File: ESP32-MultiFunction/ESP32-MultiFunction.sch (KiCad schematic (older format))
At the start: 8 parts, among them U0 ESP32_DEVKIT_C

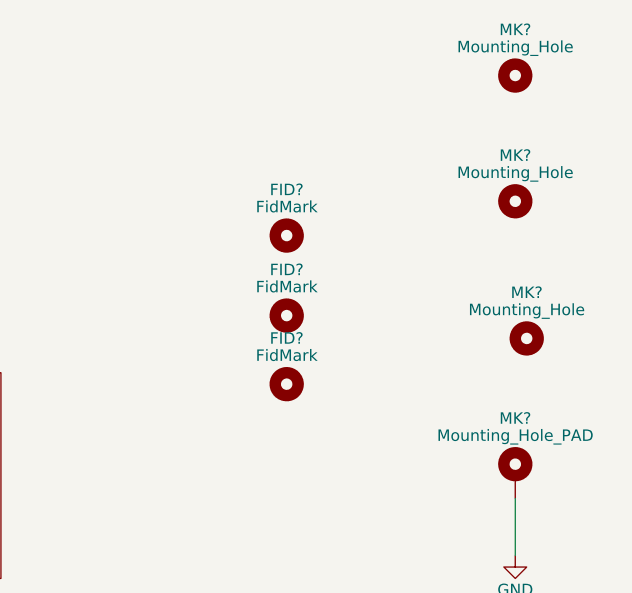
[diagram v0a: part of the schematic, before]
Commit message: Working on ESP32-MultiFunction.
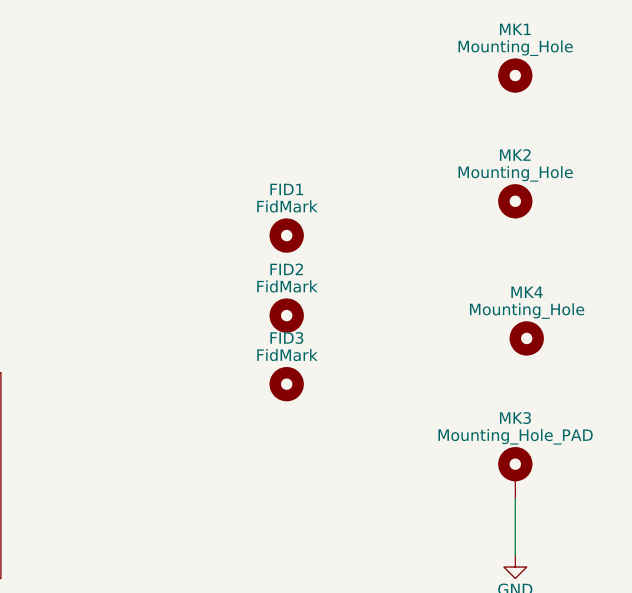
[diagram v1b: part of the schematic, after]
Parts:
- FID1, FID2, FID3: renamed from FID?; footprint (none) -> Fiducials:Fiducial_1mm_Dia_2.54mm_Outer_CopperBottom
- MK1, MK2, MK4: renamed from MK?; footprint (none) -> Mounting_Holes:MountingHole_3.2mm_M3
- MK3: renamed from MK?; footprint (none) -> Mounting_Holes:MountingHole_3.2mm_M3_Pad
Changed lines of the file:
@@
 $Descr A4 11693 8268
 encoding utf-8
-Sheet 1 7
+Sheet 1 8
 Title "ESP32 Multifunction board"
 Date ""
@@
 $EndComp
 $Comp
-L GND #PWR?
+L GND #PWR5
 U 1 1 60CCB9BA
 P 3900 2300
-F 0 "#PWR?" H 3900 2050 50  0001 C CNN
+F 0 "#PWR5" H 3900 2050 50  0001 C CNN
 F 1 "GND" H 3900 2150 50  0000 C CNN
 F 2 "" H 3900 2300 50  0001 C CNN
@@
 $EndComp
 $Comp
-L GND #PWR?
+L GND #PWR4
 U 1 1 60CCB9E8
 P 3900 2000
-F 0 "#PWR?" H 3900 1750 50  0001 C CNN
+F 0 "#PWR4" H 3900 1750 50  0001 C CNN
 F 1 "GND" H 3900 1850 50  0000 C CNN
 F 2 "" H 3900 2000 50  0001 C CNN
@@
 $EndComp
 $Comp
-L GND #PWR?
+L GND #PWR3
 U 1 1 60CCBA16
 P 2800 2650
-F 0 "#PWR?" H 2800 2400 50  0001 C CNN
+F 0 "#PWR3" H 2800 2400 50  0001 C CNN
 F 1 "GND" H 2800 2500 50  0000 C CNN
 F 2 "" H 2800 2650 50  0001 C CNN
@@
 $EndComp
 $Comp
-L +3V3 #PWR?
+L +3V3 #PWR2
 U 1 1 60CCBA34
 P 2800 2000
-F 0 "#PWR?" H 2800 1850 50  0001 C CNN
+F 0 "#PWR2" H 2800 1850 50  0001 C CNN
 F 1 "+3V3" H 2800 2140 50  0000 C CNN
 F 2 "" H 2800 2000 50  0001 C CNN
@@
 $EndComp
 $Comp
-L +5V #PWR?
+L +5V #PWR1
 U 1 1 60CCBAA7
 P 2550 2900
-F 0 "#PWR?" H 2550 2750 50  0001 C CNN
+F 0 "#PWR1" H 2550 2750 50  0001 C CNN
 F 1 "+5V" H 2550 3040 50  0000 C CNN
 F 2 "" H 2550 2900 50  0001 C CNN
@@
 $EndSheet
 $Comp
-L Mounting_Hole MK?
+L Mounting_Hole MK1
 U 1 1 60CD4484
 P 10450 1000
-F 0 "MK?" H 10450 1200 50  0000 C CNN
+F 0 "MK1" H 10450 1200 50  0000 C CNN
 F 1 "Mounting_Hole" H 10450 1125 50  0000 C CNN
-F 2 "" H 10450 1000 50  0001 C CNN
+F 2 "Mounting_Holes:MountingHole_3.2mm_M3" H 10450 1000 50  0001 C CNN
 F 3 "" H 10450 1000 50  0001 C CNN
 	1    10450 1000
@@
 $EndComp
 $Comp
-L Mounting_Hole MK?
+L Mounting_Hole MK2
 U 1 1 60CD44E3
 P 10450 1550
-F 0 "MK?" H 10450 1750 50  0000 C CNN
+F 0 "MK2" H 10450 1750 50  0000 C CNN
 F 1 "Mounting_Hole" H 10450 1675 50  0000 C CNN
-F 2 "" H 10450 1550 50  0001 C CNN
+F 2 "Mounting_Holes:MountingHole_3.2mm_M3" H 10450 1550 50  0001 C CNN
 F 3 "" H 10450 1550 50  0001 C CNN
 	1    10450 1550
@@
 $EndComp
 $Comp
-L Mounting_Hole MK?
+L Mounting_Hole MK4
 U 1 1 60CD4516
 P 10500 2150
-F 0 "MK?" H 10500 2350 50  0000 C CNN
+F 0 "MK4" H 10500 2350 50  0000 C CNN
 F 1 "Mounting_Hole" H 10500 2275 50  0000 C CNN
-F 2 "" H 10500 2150 50  0001 C CNN
+F 2 "Mounting_Holes:MountingHole_3.2mm_M3" H 10500 2150 50  0001 C CNN
 F 3 "" H 10500 2150 50  0001 C CNN
 	1    10500 2150
@@
 $EndComp
 $Comp
-L Mounting_Hole_PAD MK?
+L Mounting_Hole_PAD MK3
 U 1 1 60CD454B
 P 10450 2750
-F 0 "MK?" H 10450 3000 50  0000 C CNN
+F 0 "MK3" H 10450 3000 50  0000 C CNN
 F 1 "Mounting_Hole_PAD" H 10450 2925 50  0000 C CNN
-F 2 "" H 10450 2750 50  0001 C CNN
+F 2 "Mounting_Holes:MountingHole_3.2mm_M3_Pad" H 10450 2750 50  0001 C CNN
 F 3 "" H 10450 2750 50  0001 C CNN
 	1    10450 2750
@@
 $EndComp
 $Comp
-L GND #PWR?
+L GND #PWR6
 U 1 1 60CD4616
 P 10450 3100
-F 0 "#PWR?" H 10450 2850 50  0001 C CNN
+F 0 "#PWR6" H 10450 2850 50  0001 C CNN
 F 1 "GND" H 10450 2950 50  0000 C CNN
 F 2 "" H 10450 3100 50  0001 C CNN
@@
 	10450 2850 10450 3100
 $Comp
-L Mounting_Hole FID?
+L Mounting_Hole FID1
 U 1 1 60CD48B9
 P 9450 1700
-F 0 "FID?" H 9450 1900 50  0000 C CNN
+F 0 "FID1" H 9450 1900 50  0000 C CNN
 F 1 "FidMark" H 9450 1825 50  0000 C CNN
-F 2 "" H 9450 1700 50  0001 C CNN
+F 2 "Fiducials:Fiducial_1mm_Dia_2.54mm_Outer_CopperBottom" H 9450 1700 50  0001 C CNN
 F 3 "" H 9450 1700 50  0001 C CNN
 	1    9450 1700
@@
 $EndComp
 $Comp
-L Mounting_Hole FID?
+L Mounting_Hole FID2
 U 1 1 60CD49DA
 P 9450 2050
-F 0 "FID?" H 9450 2250 50  0000 C CNN
+F 0 "FID2" H 9450 2250 50  0000 C CNN
 F 1 "FidMark" H 9450 2175 50  0000 C CNN
-F 2 "" H 9450 2050 50  0001 C CNN
+F 2 "Fiducials:Fiducial_1mm_Dia_2.54mm_Outer_CopperBottom" H 9450 2050 50  0001 C CNN
 F 3 "" H 9450 2050 50  0001 C CNN
 	1    9450 2050
@@
 $EndComp
 $Comp
-L Mounting_Hole FID?
+L Mounting_Hole FID3
 U 1 1 60CD4A15
 P 9450 2350
-F 0 "FID?" H 9450 2550 50  0000 C CNN
+F 0 "FID3" H 9450 2550 50  0000 C CNN
 F 1 "FidMark" H 9450 2475 50  0000 C CNN
-F 2 "" H 9450 2350 50  0001 C CNN
+F 2 "Fiducials:Fiducial_1mm_Dia_2.54mm_Outer_CopperBottom" H 9450 2350 50  0001 C CNN
 F 3 "" H 9450 2350 50  0001 C CNN
 	1    9450 2350

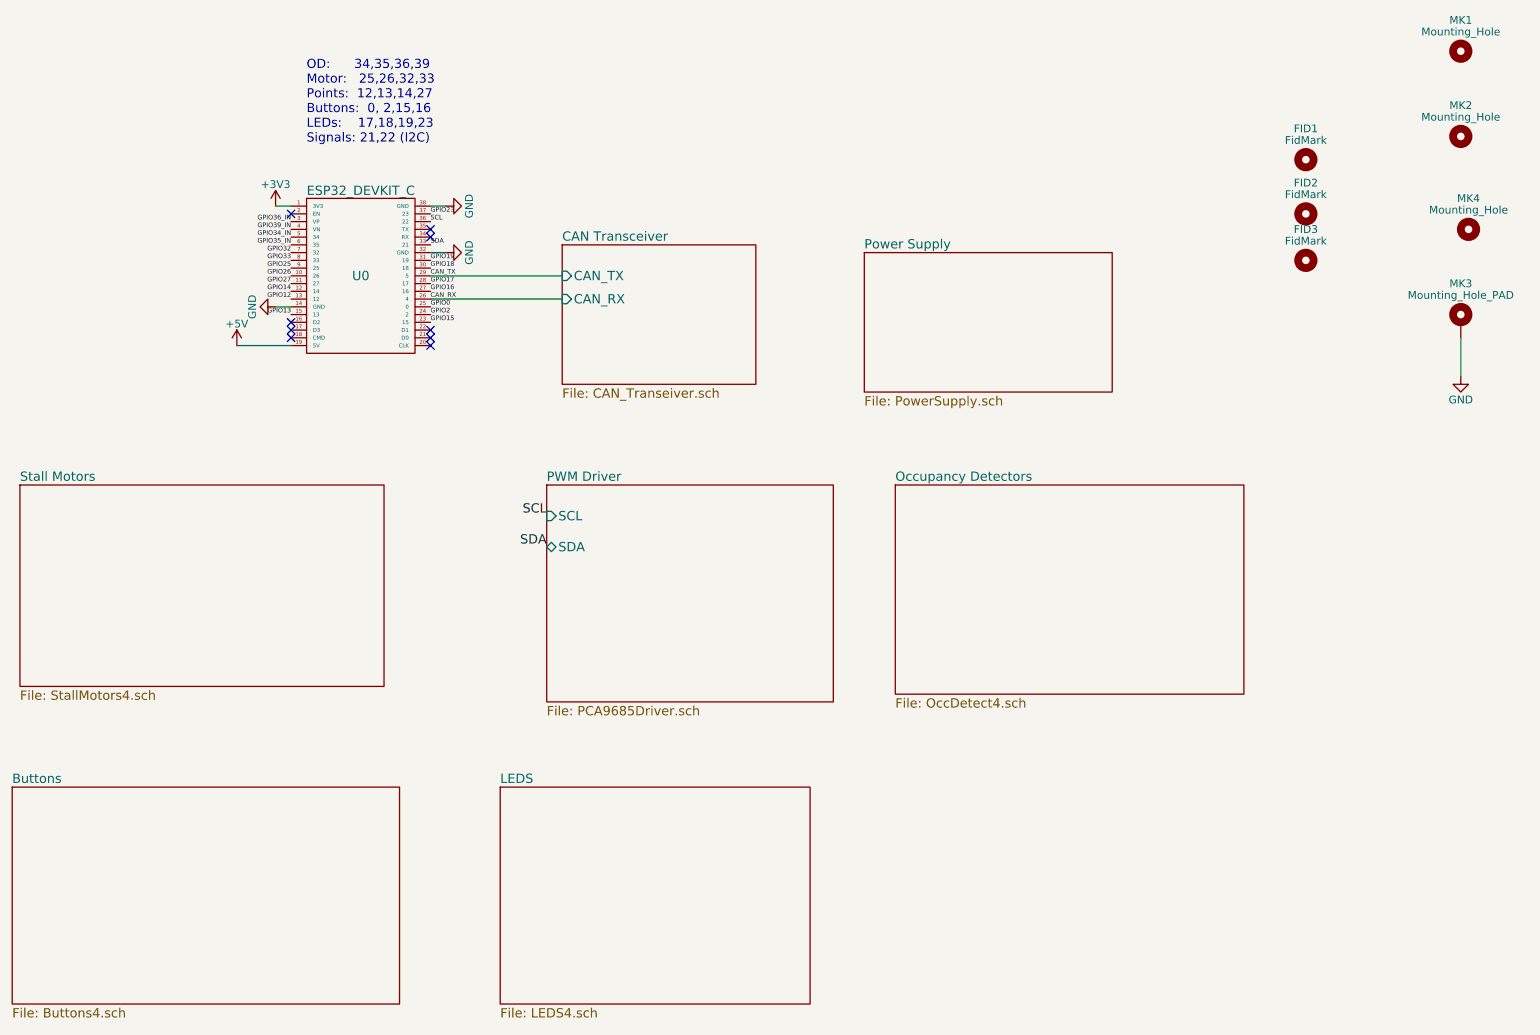
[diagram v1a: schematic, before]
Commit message: Working on ESP32-MultiFunction.
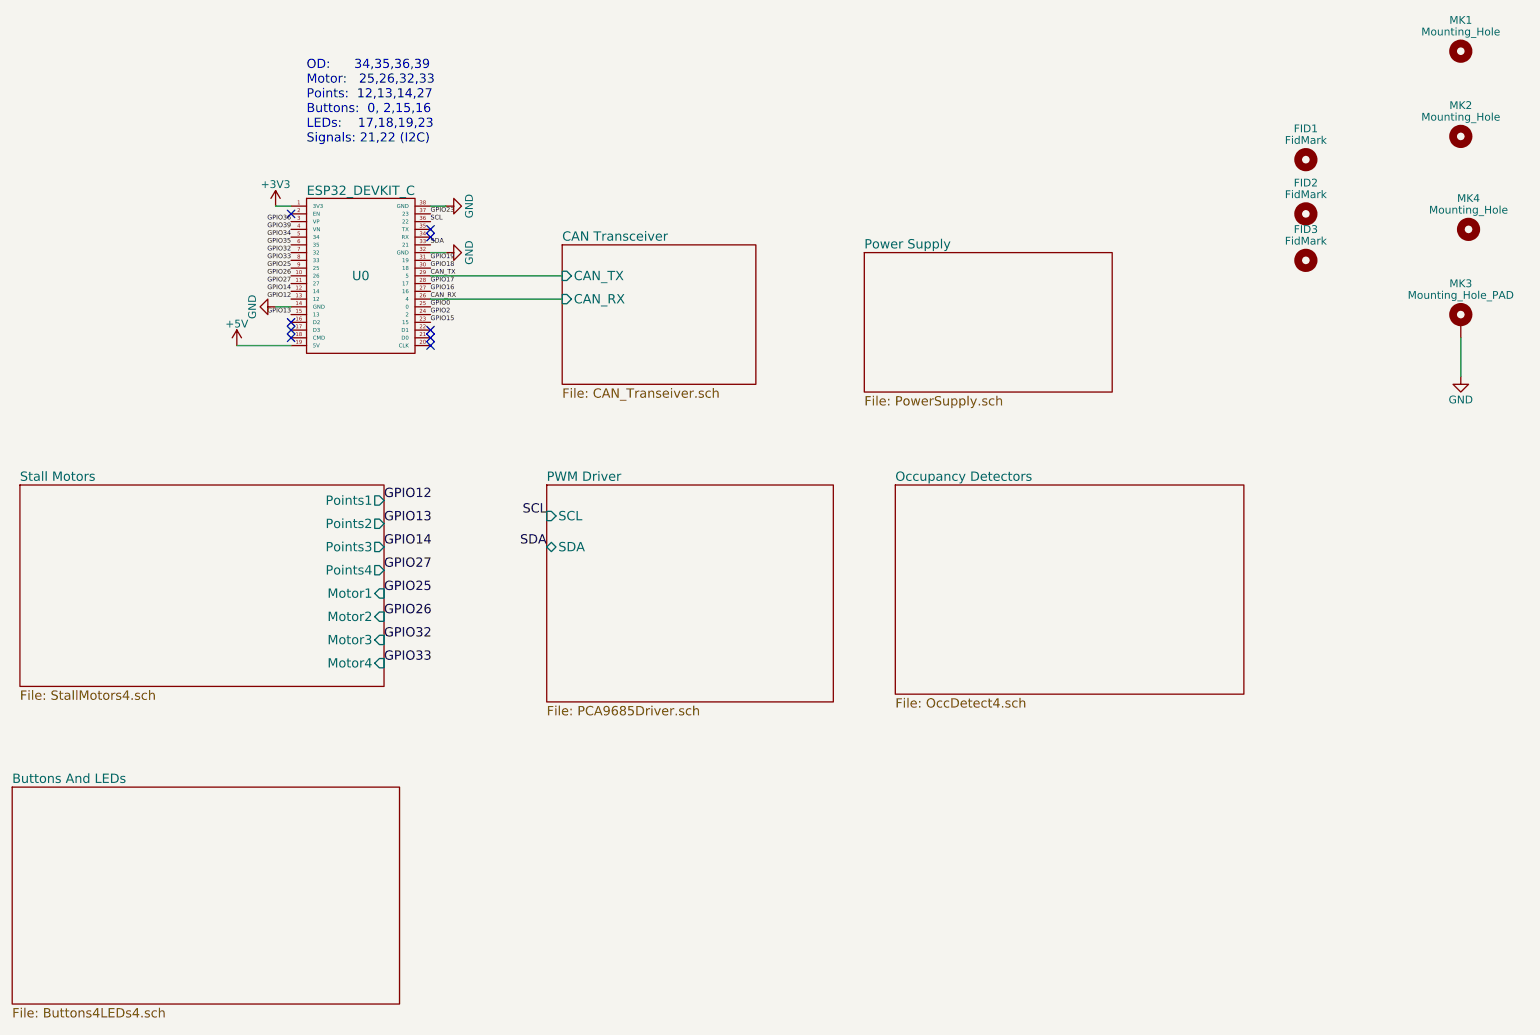
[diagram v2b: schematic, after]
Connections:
- net GPIO34_IN renamed GPIO34
- net GPIO35_IN renamed GPIO35
- net GPIO36_IN renamed GPIO36
- net GPIO39_IN renamed GPIO39
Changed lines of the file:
@@
 $Descr A4 11693 8268
 encoding utf-8
-Sheet 1 8
+Sheet 1 7
 Title "ESP32 Multifunction board"
 Date ""
@@
 NoConn ~ 3800 2900
 Text Label 2900 2100 2    30   ~ 0
-GPIO36_IN
+GPIO36
 Text Label 2900 2150 2    30   ~ 0
-GPIO39_IN
+GPIO39
 Text Label 2900 2200 2    30   ~ 0
-GPIO34_IN
+GPIO34
 Text Label 2900 2250 2    30   ~ 0
-GPIO35_IN
+GPIO35
 Text Label 2900 2300 2    30   ~ 0
 GPIO32
@@
 F0 "Stall Motors" 60
 F1 "StallMotors4.sch" 60
+F2 "Points1" O R 3500 3900 60
+F3 "Points2" O R 3500 4050 60
+F4 "Points3" O R 3500 4200 60
+F5 "Points4" O R 3500 4350 60
+F6 "Motor1" I R 3500 4500 60
+F7 "Motor2" I R 3500 4650 60
+F8 "Motor3" I R 3500 4800 60
+F9 "Motor4" I R 3500 4950 60
 $EndSheet
 $Sheet
 S 1100 5750 2500 1400
 U 60CD423F
-F0 "Buttons" 60
-F1 "Buttons4.sch" 60
-$EndSheet
-$Sheet
-S 4250 5750 2000 1400
-U 60CD424F
-F0 "LEDS" 60
-F1 "LEDS4.sch" 60
+F0 "Buttons And LEDs" 60
+F1 "Buttons4LEDs4.sch" 60
 $EndSheet
 $Comp
@@
 	1    0    0    -1
 $EndComp
+Text Label 3500 3900 0    60   ~ 0
+GPIO12
+Text Label 3500 4050 0    60   ~ 0
+GPIO13
+Text Label 3500 4200 0    60   ~ 0
+GPIO14
+Text Label 3500 4350 0    60   ~ 0
+GPIO27
+Text Label 3500 4500 0    60   ~ 0
+GPIO25
+Text Label 3500 4650 0    60   ~ 0
+GPIO26
+Text Label 3500 4800 0    60   ~ 0
+GPIO32
+Text Label 3500 4950 0    60   ~ 0
+GPIO33
 $EndSCHEMATC

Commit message: Working on ESP32-MultiFunction.
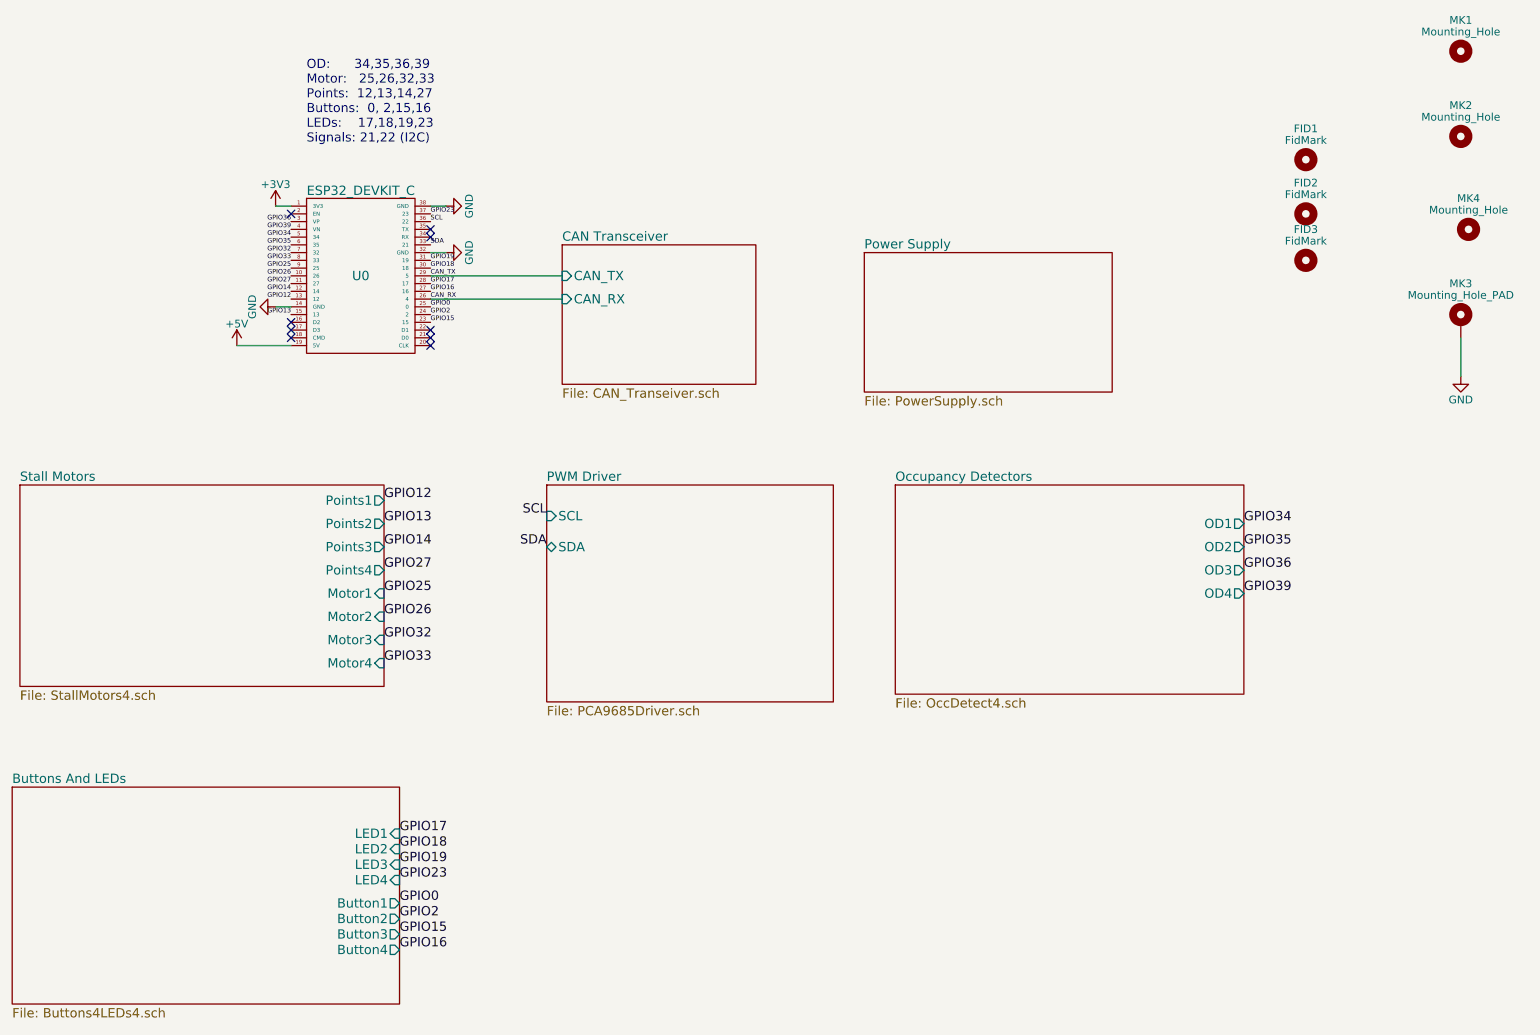
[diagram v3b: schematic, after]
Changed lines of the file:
@@
 $EndComp
 $Comp
-L GND #PWR5
+L GND #PWR01
 U 1 1 60CCB9BA
 P 3900 2300
-F 0 "#PWR5" H 3900 2050 50  0001 C CNN
+F 0 "#PWR01" H 3900 2050 50  0001 C CNN
 F 1 "GND" H 3900 2150 50  0000 C CNN
 F 2 "" H 3900 2300 50  0001 C CNN
@@
 $EndComp
 $Comp
-L GND #PWR4
+L GND #PWR02
 U 1 1 60CCB9E8
 P 3900 2000
-F 0 "#PWR4" H 3900 1750 50  0001 C CNN
+F 0 "#PWR02" H 3900 1750 50  0001 C CNN
 F 1 "GND" H 3900 1850 50  0000 C CNN
 F 2 "" H 3900 2000 50  0001 C CNN
@@
 $EndComp
 $Comp
-L GND #PWR3
+L GND #PWR03
 U 1 1 60CCBA16
 P 2800 2650
-F 0 "#PWR3" H 2800 2400 50  0001 C CNN
+F 0 "#PWR03" H 2800 2400 50  0001 C CNN
 F 1 "GND" H 2800 2500 50  0000 C CNN
 F 2 "" H 2800 2650 50  0001 C CNN
@@
 $EndComp
 $Comp
-L +3V3 #PWR2
+L +3V3 #PWR04
 U 1 1 60CCBA34
 P 2800 2000
-F 0 "#PWR2" H 2800 1850 50  0001 C CNN
+F 0 "#PWR04" H 2800 1850 50  0001 C CNN
 F 1 "+3V3" H 2800 2140 50  0000 C CNN
 F 2 "" H 2800 2000 50  0001 C CNN
@@
 $EndComp
 $Comp
-L +5V #PWR1
+L +5V #PWR05
 U 1 1 60CCBAA7
 P 2550 2900
-F 0 "#PWR1" H 2550 2750 50  0001 C CNN
+F 0 "#PWR05" H 2550 2750 50  0001 C CNN
 F 1 "+5V" H 2550 3040 50  0000 C CNN
 F 2 "" H 2550 2900 50  0001 C CNN
@@
 F0 "Occupancy Detectors" 60
 F1 "OccDetect4.sch" 60
+F2 "OD1" O R 9050 4050 60
+F3 "OD2" O R 9050 4200 60
+F4 "OD3" O R 9050 4350 60
+F5 "OD4" O R 9050 4500 60
 $EndSheet
 $Sheet
@@
 F0 "Buttons And LEDs" 60
 F1 "Buttons4LEDs4.sch" 60
+F2 "LED1" I R 3600 6050 60
+F3 "LED2" I R 3600 6150 60
+F4 "LED3" I R 3600 6250 60
+F5 "LED4" I R 3600 6350 60
+F6 "Button1" O R 3600 6500 60
+F7 "Button2" O R 3600 6600 60
+F8 "Button3" O R 3600 6700 60
+F9 "Button4" O R 3600 6800 60
 $EndSheet
 $Comp
@@
 $EndComp
 $Comp
-L GND #PWR6
+L GND #PWR06
 U 1 1 60CD4616
 P 10450 3100
-F 0 "#PWR6" H 10450 2850 50  0001 C CNN
+F 0 "#PWR06" H 10450 2850 50  0001 C CNN
 F 1 "GND" H 10450 2950 50  0000 C CNN
 F 2 "" H 10450 3100 50  0001 C CNN
@@
 Text Label 3500 4950 0    60   ~ 0
 GPIO33
+Text Label 9050 4050 0    60   ~ 0
+GPIO34
+Text Label 9050 4200 0    60   ~ 0
+GPIO35
+Text Label 9050 4350 0    60   ~ 0
+GPIO36
+Text Label 9050 4500 0    60   ~ 0
+GPIO39
+Text Label 3600 6500 0    60   ~ 0
+GPIO0
+Text Label 3600 6600 0    60   ~ 0
+GPIO2
+Text Label 3600 6700 0    60   ~ 0
+GPIO15
+Text Label 3600 6800 0    60   ~ 0
+GPIO16
+Text Label 3600 6050 0    60   ~ 0
+GPIO17
+Text Label 3600 6150 0    60   ~ 0
+GPIO18
+Text Label 3600 6250 0    60   ~ 0
+GPIO19
+Text Label 3600 6350 0    60   ~ 0
+GPIO23
 $EndSCHEMATC
